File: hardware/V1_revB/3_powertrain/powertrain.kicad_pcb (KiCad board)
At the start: 2 copper layers, 39.1 x 44.7 mm, 25 parts, among them J6 , SW1 SKRHADE010

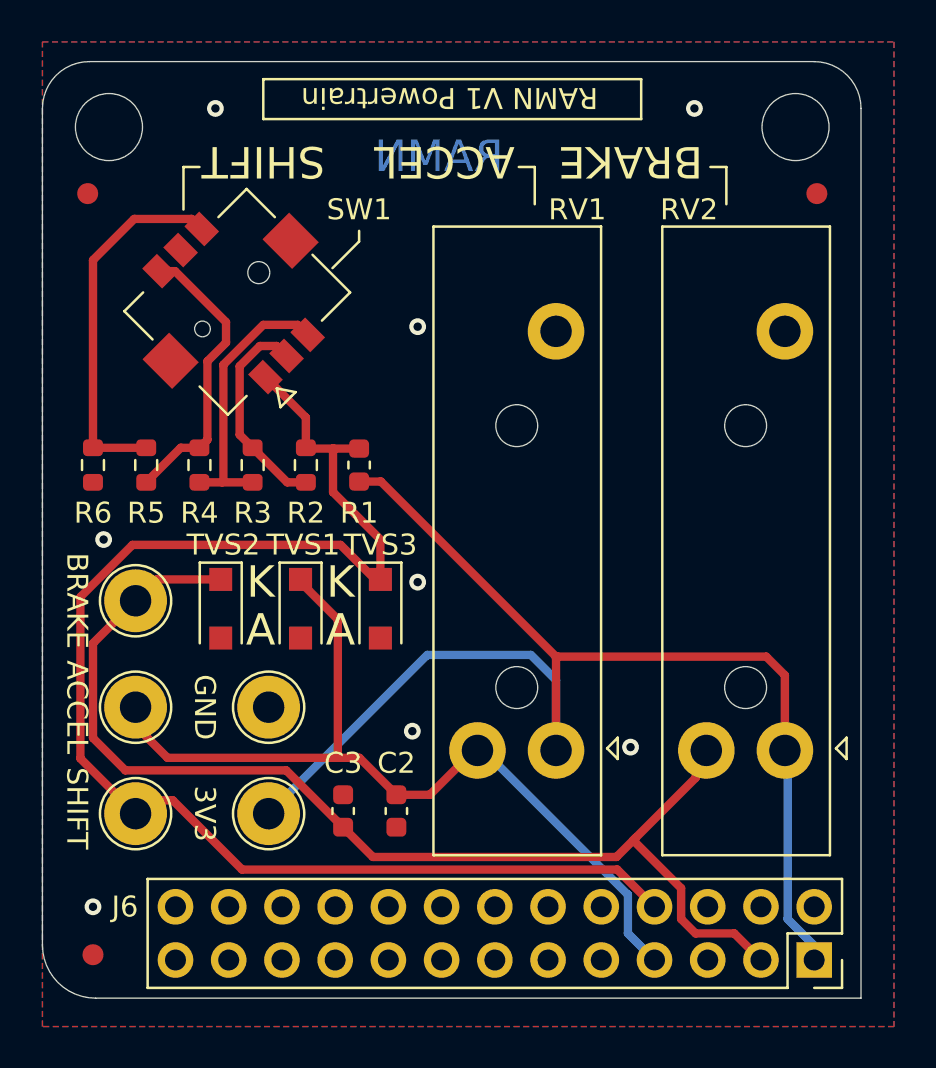
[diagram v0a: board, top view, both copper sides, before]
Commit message: feat (hw): change USB to USB C and change Test points footprints
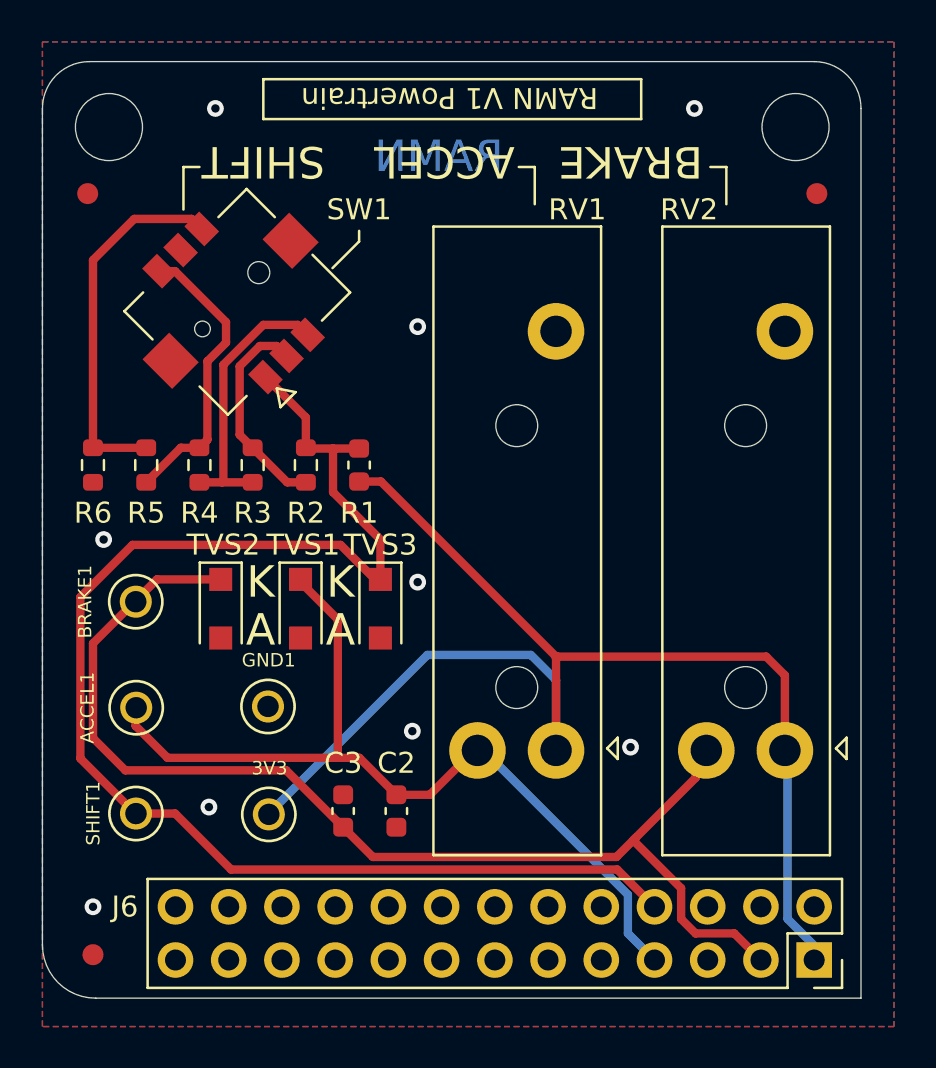
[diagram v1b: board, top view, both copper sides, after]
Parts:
- removed ACCEL, BRAKE, GND, SHIFT: TestPoint, TestPoint:TestPoint_Loop_D2.54mm_Drill1.5mm_Beaded
- added ACCEL1: TestPoint, Global_Library:KEYSTONE_5002, F.Cu at (36.9, 51.5)
- added BRAKE1: TestPoint, Global_Library:KEYSTONE_5002, F.Cu at (36.8, 46.4)
- added GND1: TestPoint, Global_Library:KEYSTONE_5002, F.Cu at (43.1, 51.4)
- added SHIFT1: TestPoint, Global_Library:KEYSTONE_5002, F.Cu at (36.9, 56.5)
- 3V3: footprint TestPoint:TestPoint_Loop_D2.54mm_Drill1.5mm_Beaded -> Global_Library:KEYSTONE_5002
- turned 3V3 to 0 degrees
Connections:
- J6 pad 10: Net-(J6-Pad10) -> unconnected-(J6-Pin_10-Pad10)
- J6 pad 11: Net-(J6-Pad11) -> unconnected-(J6-Pin_11-Pad11)
- J6 pad 12: Net-(J6-Pad12) -> unconnected-(J6-Pin_12-Pad12)
- J6 pad 13: Net-(J6-Pad13) -> unconnected-(J6-Pin_13-Pad13)
- J6 pad 14: Net-(J6-Pad14) -> unconnected-(J6-Pin_14-Pad14)
- J6 pad 15: Net-(J6-Pad15) -> unconnected-(J6-Pin_15-Pad15)
- J6 pad 16: Net-(J6-Pad16) -> unconnected-(J6-Pin_16-Pad16)
- J6 pad 17: Net-(J6-Pad17) -> unconnected-(J6-Pin_17-Pad17)
- J6 pad 18: Net-(J6-Pad18) -> unconnected-(J6-Pin_18-Pad18)
- J6 pad 19: Net-(J6-Pad19) -> unconnected-(J6-Pin_19-Pad19)
- J6 pad 20: Net-(J6-Pad20) -> unconnected-(J6-Pin_20-Pad20)
- J6 pad 21: Net-(J6-Pad21) -> unconnected-(J6-Pin_21-Pad21)
- J6 pad 22: Net-(J6-Pad22) -> unconnected-(J6-Pin_22-Pad22)
- J6 pad 23: Net-(J6-Pad23) -> unconnected-(J6-Pin_23-Pad23)
- J6 pad 24: Net-(J6-Pad24) -> unconnected-(J6-Pin_24-Pad24)
- J6 pad 25: Net-(J6-Pad25) -> unconnected-(J6-Pin_25-Pad25)
- J6 pad 26: Net-(J6-Pad26) -> unconnected-(J6-Pin_26-Pad26)
- J6 pad 5: Net-(J6-Pad5) -> unconnected-(J6-Pin_5-Pad5)
- J6 pad 6: Net-(J6-Pad6) -> unconnected-(J6-Pin_6-Pad6)
- J6 pad 9: Net-(J6-Pad9) -> unconnected-(J6-Pin_9-Pad9)
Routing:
- net JOYSTICK: track 68.9 -> 68.3 mm
- net GND: vias 8 -> 9
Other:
- net class Default removed
